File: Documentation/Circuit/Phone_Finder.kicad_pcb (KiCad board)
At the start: 2 copper layers, 28.6 x 50.8 mm, 16 parts, among them P1 CONN_5X2, U1 BLE112, U2 TPS62730, U3 AT42QT1011

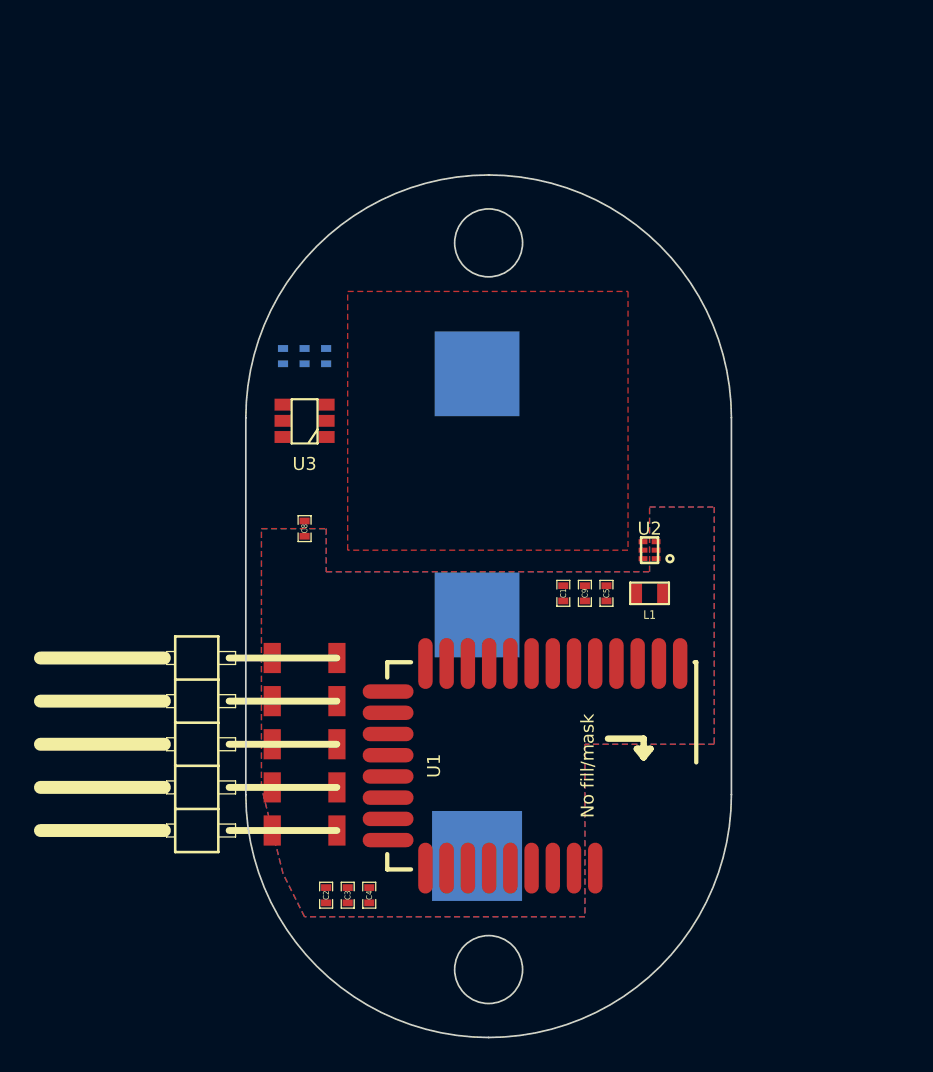
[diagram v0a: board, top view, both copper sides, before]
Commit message: Modified input circuitry, remade PCB
Changed input circuit from Atmel's QTouch chipset to a simple momentary
pushbutton, added datasheet for said pushbutton.  Button is dust tight
and waterproof as per spec doc.

Changed passives to use 0603 footprint instead of 0402 to provide easier
reflowing.

Performed initial layout, connectivity, and ground pours.

Still pending are circuit connectivity and feasibility, and PCB
connectivity checks.  Parts might be purchased at this point.  Parts
will then be compared against footprints to ensure fit before sending
gerbers (and order) off to PCB fab.
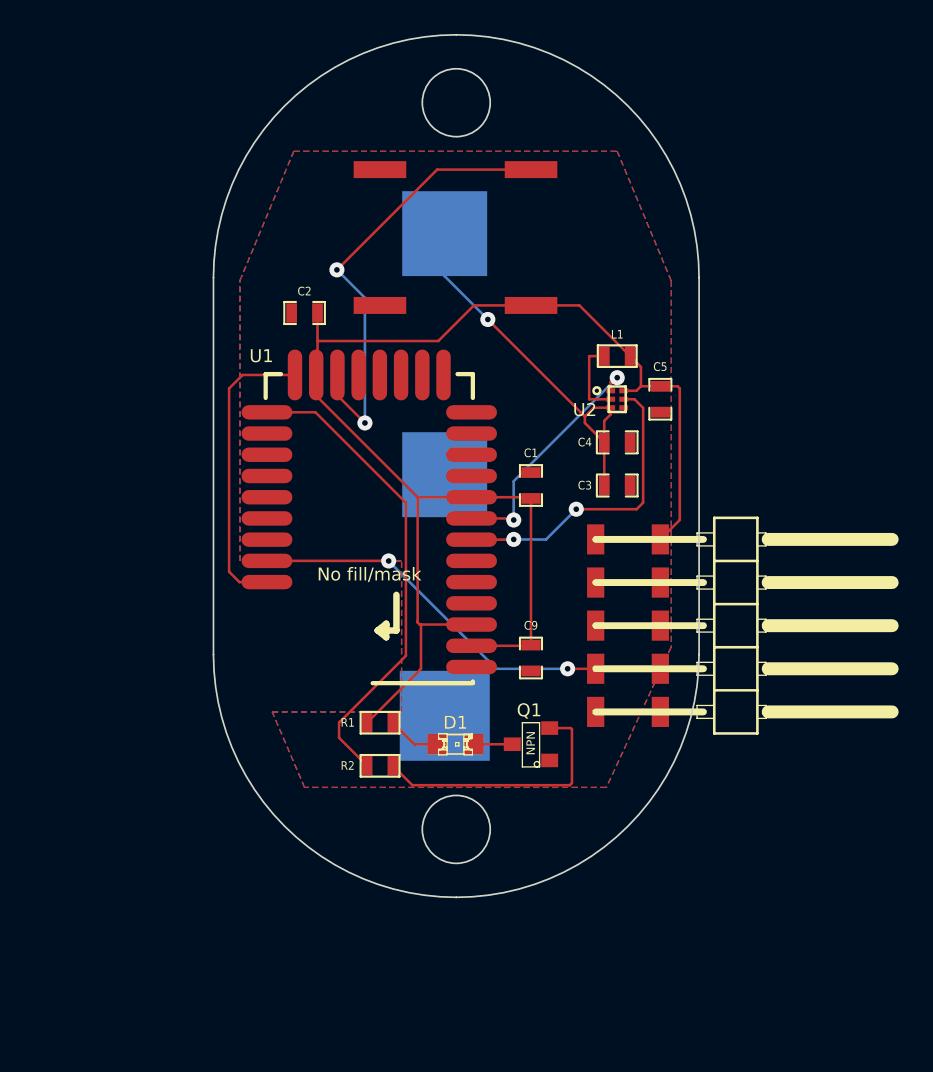
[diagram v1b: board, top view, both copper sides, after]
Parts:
- removed C6: Cx, SM0402
- removed C7: Cs, SM0402
- removed C8: 0.1uF, SM0402
- removed U3: AT42QT1011, SOT23_6
- added D1: LED, LED-0805, F.Cu at (146.1, 100.3)
- added Q1: NPN, SOT23, F.Cu at (150.5, 100.3)
- added R2: 10k, SM0603, F.Cu at (141.6, 101.6)
- added SW1: SPST, KSC_GULLWING, F.Cu at (146.1, 70.5)
- BT1: value BATTERY -> Replace with CR2032
- C1, C2, C3, C4, C5, C9: footprint SM0402 -> SM0603_Capa
- R1: value Rs -> R; footprint SM0402 -> SM0603; moved to F.Cu
- moved P1 36.1 mm to (163.2, 89.5), turned to 270 degrees
- moved C2 34.3 mm to (137.2, 74.9), turned to 180 degrees
- moved C4 30.4 mm to (155.6, 82.5), turned to 0 degrees
- moved C3 28.9 mm to (155.6, 85.1), turned to 0 degrees
- moved R1 22.3 mm to (141.6, 99.1), turned to 0 degrees
- moved U1 17.3 mm to (141.0, 87.6), turned to 180 degrees
- moved L1 14.1 mm to (155.6, 77.5), turned to 180 degrees
- moved C5 11.9 mm to (158.1, 80.0)
- moved U2 9.09 mm to (155.6, 80.0), turned to 0 degrees
- moved BT1 8.47 mm to (145.4, 84.5)
- moved C1 6.63 mm to (150.5, 85.1), turned to 90 degrees
- moved C9 4.96 mm to (150.5, 95.2)
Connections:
- R1 pad 1: N-0000034 (its old number) -> VDD
- U1 pad 18: /User Input/TOUCH_MODE -> (no net)
- U1 pad 22: (no net) -> /User Input/STATUS_LED
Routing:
- net VDD: track 0.00 -> 85.3 mm
- net /User Input/STATUS_LED: track 0.00 -> 28.2 mm
- net /User Input/TOUCH_OUT: track 0.00 -> 27.1 mm, vias 0 -> 2
- net +BATT: track 0.00 -> 22.7 mm, vias 0 -> 1
- net /RESET_N: track 0.00 -> 22.0 mm, vias 0 -> 2
- net /Power Supply/DCDC: track 0.00 -> 17.9 mm, vias 0 -> 2
- net GND: track 0.00 -> 17.5 mm
- net N-0000036: track 0.00 -> 15.6 mm
- net /Power Supply/STAT: track 0.00 -> 14.4 mm, vias 0 -> 2
- net N-0000032: track 0.00 -> 4.69 mm
- net N-0000034: track 0.00 -> 3.16 mm
- net N-0000035: track 0.00 -> 2.30 mm
- removed copper zone on F.Cu, net N-0000034 (its old number)
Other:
- net class Default: clearance 0.254 -> 0.1524; trace_width 0.254 -> 0.1524; via_drill 0.635 -> 0.3302
- net class Power added: clearance 0.1524, trace_width 0.3048, via_dia 0.889, via_drill 0.3302
- rule trace_clearance: 0.254 -> 0.1524
